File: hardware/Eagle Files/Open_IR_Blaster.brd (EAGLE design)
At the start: 60 x 60 mm, 36 parts, among them J1 4907, Q1 IRLML6344TRPBF, U1 AZ1117EH-1.5TRG1

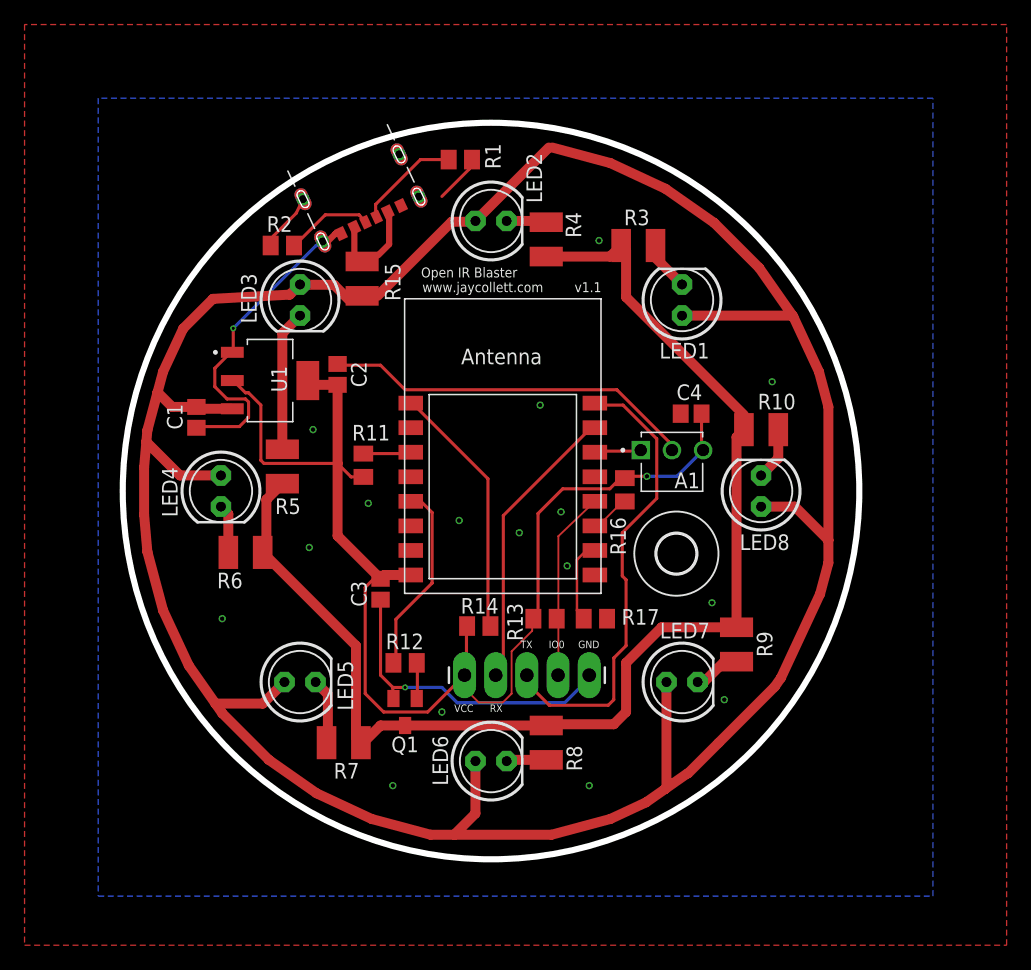
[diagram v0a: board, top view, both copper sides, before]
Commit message: Adds indicator LED to board and pulldown for MOSFET (not required).
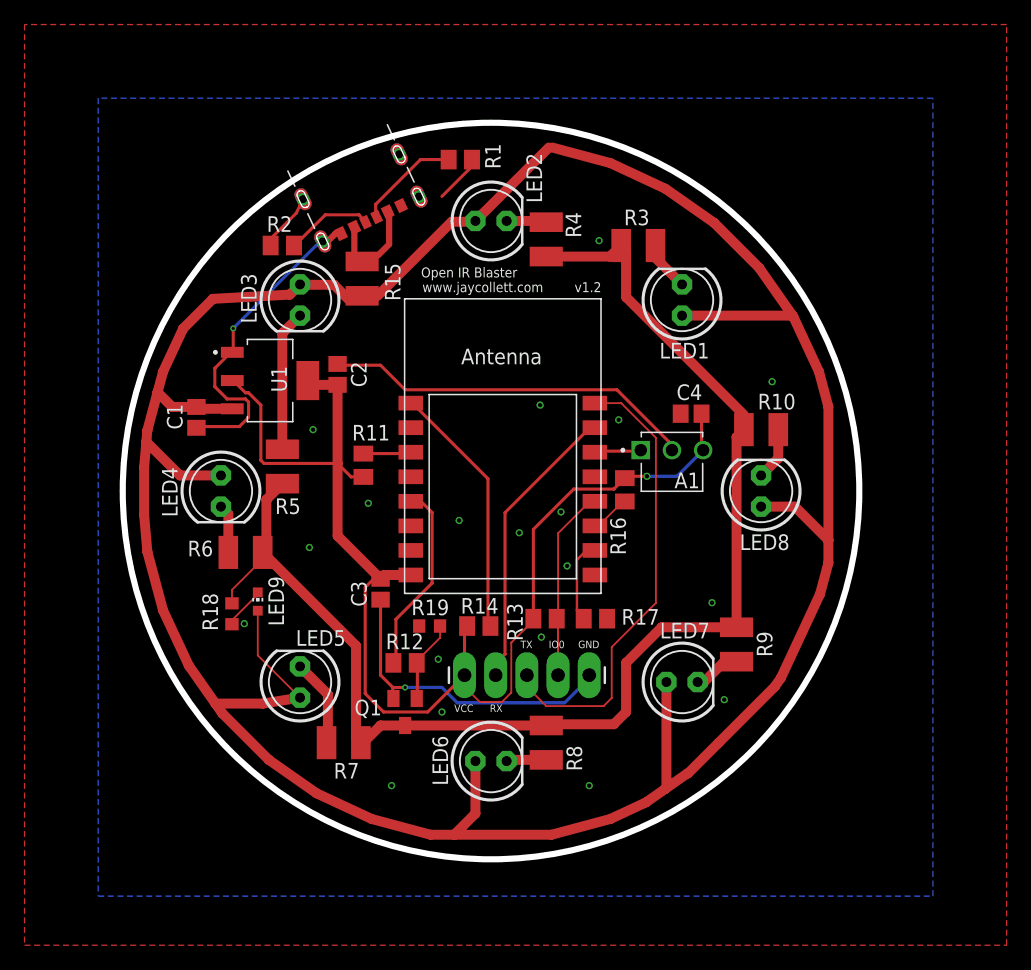
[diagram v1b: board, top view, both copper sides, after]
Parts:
- removed H1: MOUNT-HOLE3.2, holes:3,2
- added LED9: (no value), adafruit:CHIP-LED0603
- added R18: 4.7k, adafruit:R0603
- added R19: 100k, adafruit:R0603
- turned LED5 to 90 degrees
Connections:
- new net N$13: LED9.C, R18.2
- net +5VDC: now also LED9.A
- net GND: now also R19.1
- net N$12: now also R19.2
- net N$9: now also R18.1
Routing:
- net +5VDC: track 230.4 -> 239.5 mm
- net N$9: track 104.1 -> 109.2 mm
- net GPIO0: track 15.6 -> 20.3 mm
- net N$12: track 2.96 -> 6.75 mm
- net N$13: track 0.00 -> 3.47 mm
- net N$5: track 5.40 -> 7.20 mm
- net +3.3VDC: track 103.2 -> 102.4 mm
- net GND: vias 18 -> 21
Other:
- board text added: "v1.2"
- board text removed: "v1.1"
